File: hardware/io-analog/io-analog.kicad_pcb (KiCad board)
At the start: 2 copper layers, 60 x 60 mm, 22 parts, among them J1 IO EXTENSION, J2 DIMMER_B, J5 12V_A, J6 12V_B, U1 LM317T, U2 74LS164, U3 TLC7226A, U4 LM324A

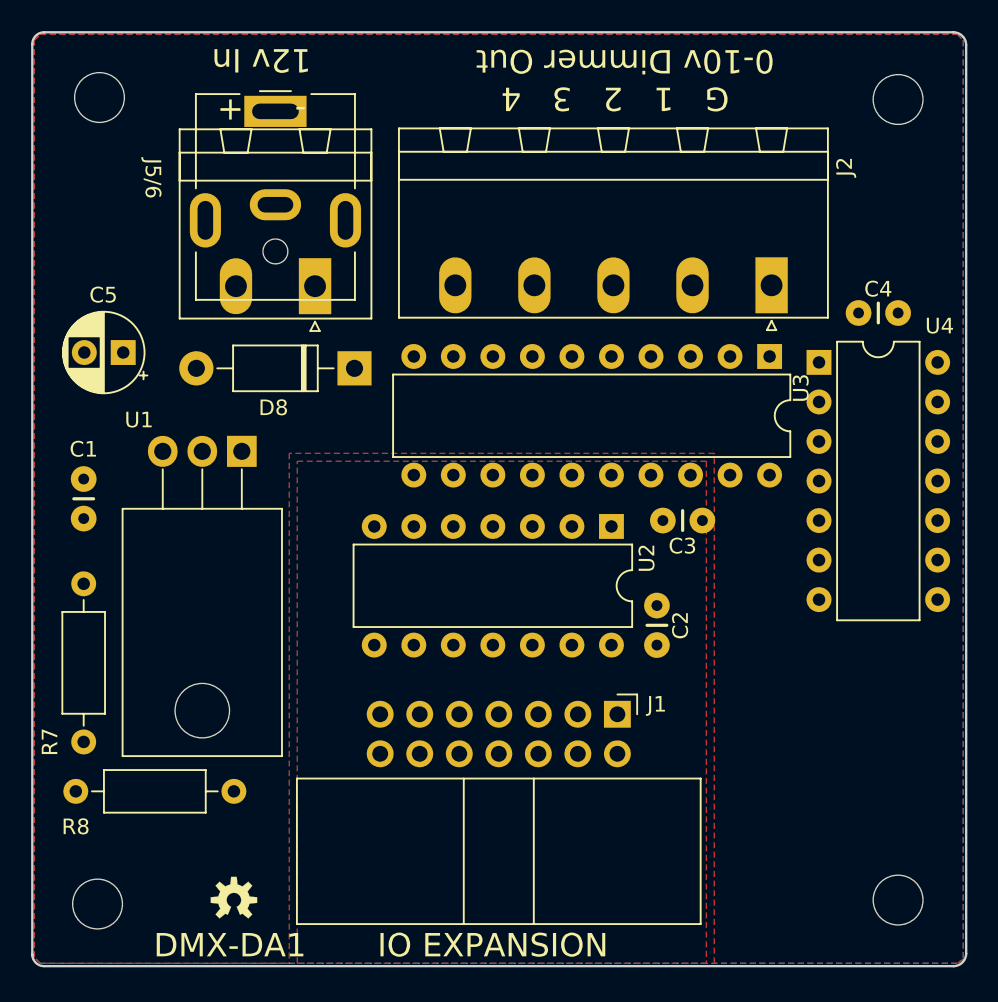
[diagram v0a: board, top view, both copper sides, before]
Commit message: Prototype version of DMX, Analog, and PWM IO Modules and both TX and RX IO interfaces.
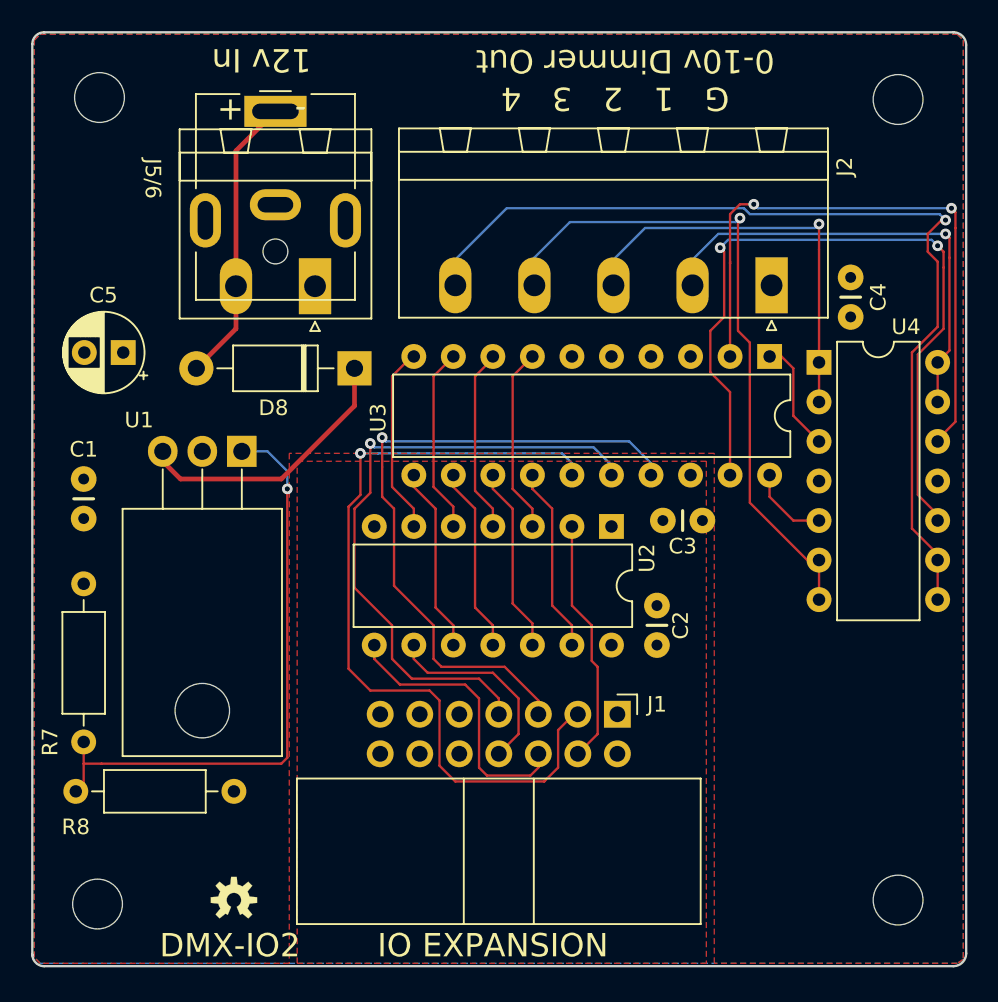
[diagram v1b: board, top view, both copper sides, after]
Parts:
- moved C4 2.05 mm to (167.0, 77.6), turned to 90 degrees
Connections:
- net Net-(J1-Pad4) renamed /SR-OUT
- net Net-(J1-Pad6) renamed /SR-CLK
- net Net-(J1-Pad8) renamed /~SR_CLR
- U2 pad 10: Net-(U2-Pad10) -> /D3
- U2 pad 11: Net-(U2-Pad11) -> /D2
- U2 pad 12: Net-(U2-Pad12) -> /D1
- U2 pad 13: Net-(U2-Pad13) -> /D0
- U2 pad 3: Net-(U2-Pad3) -> /D7
- U2 pad 4: Net-(U2-Pad4) -> /D6
- U2 pad 5: Net-(U2-Pad5) -> /D5
- U2 pad 6: Net-(U2-Pad6) -> /D4
- U3 pad 10: Net-(U2-Pad10) -> /D4
- U3 pad 11: Net-(U2-Pad6) -> /D3
- U3 pad 12: Net-(U2-Pad5) -> /D2
- U3 pad 13: Net-(U2-Pad4) -> /D1
- U3 pad 14: Net-(U2-Pad3) -> /D0
- U3 pad 7: Net-(U2-Pad13) -> /D7
- U3 pad 8: Net-(U2-Pad12) -> /D6
- U3 pad 9: Net-(U2-Pad11) -> /D5
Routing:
- net Net-(J2-Pad5): track 0.00 -> 61.5 mm, vias 0 -> 1
- net /~WR: track 0.00 -> 52.4 mm, vias 0 -> 1
- net /AO3: track 0.00 -> 49.0 mm, vias 0 -> 2
- net Net-(J2-Pad4): track 0.00 -> 43.2 mm, vias 0 -> 1
- net /A0: track 0.00 -> 43.0 mm, vias 0 -> 1
- net /A1: track 0.00 -> 40.9 mm, vias 0 -> 1
- net /AO0: track 0.00 -> 39.4 mm, vias 0 -> 2
- net Net-(R7-Pad1): track 0.00 -> 38.5 mm, vias 0 -> 1
- net Net-(J2-Pad2): track 0.00 -> 29.8 mm, vias 0 -> 1
- net Net-(J2-Pad3): track 0.00 -> 27.2 mm, vias 0 -> 1
- net Net-(D8-Pad2): track 0.00 -> 18.6 mm
- net /SR-CLK: track 0.00 -> 18.2 mm
- net Net-(D8-Pad1): track 0.00 -> 17.8 mm
- net /SR-OUT: track 0.00 -> 15.8 mm
- net /~SR_CLR: track 0.00 -> 12.8 mm
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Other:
- net class Power added: clearance 0.1524, trace_width 0.3048, via_dia 1.27, via_drill 0.635
- board text added: "DMX-IO2"
- board text added: "DMX-IO2, Rev 1.1 Crazy Giraffe Software"
- board text removed: "DMX-DA1"
- board text removed: "DMX-DA1, Rev 1.1 Crazy Giraffe Software"
